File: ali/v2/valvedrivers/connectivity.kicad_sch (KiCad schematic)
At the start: 27 parts, among them J7 Conn_01x03, J8 Vertical Ethernet, U4 TJA1462ATK, U5 LAN8742AI, Y2 25 MHz

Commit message: Globally remove LCSC labels, update MPNs and IOCs, add +5V monitoring to DAQs, fix some footprints
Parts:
- C24: MPN GRM21A5C2J471FWA1 -> GRM1885C1H471JA01
- C26: MPN GRM21AR72A224KAC5 -> GRM188R71H224KAC4
- J8: LCSC C34677 -> (none)
- R17, R19: MPN RC0603FR-0710KL -> RC0603FR-0710KL
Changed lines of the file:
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@@
 			)
 		)
-		(property "MPN" " RC0603FR-0710KL"
+		(property "MPN" "RC0603FR-0710KL"
 			(at 53.34 85.09 90)
 			(hide yes)
@@
 			)
 		)
-		(property "LCSC" "C34677"
-			(at 187.96 121.92 0)
-			(hide yes)
-			(show_name no)
-			(do_not_autoplace no)
-			(effects
-				(font
-					(size 1.27 1.27)
-				)
-			)
-		)
 		(pin "1"
 		)
@@
 			)
 		)
-		(property "MPN" "GRM21AR72A224KAC5"
+		(property "MPN" "GRM188R71H224KAC4"
 			(at 157.48 132.08 0)
 			(hide yes)
@@
 			)
 		)
-		(property "MPN" "GRM21A5C2J471FWA1"
+		(property "MPN" "GRM1885C1H471JA01"
 			(at 100.33 50.8 0)
 			(hide yes)
@@
 			)
 		)
-		(property "MPN" " RC0603FR-0710KL"
+		(property "MPN" "RC0603FR-0710KL"
 			(at 99.06 102.87 0)
 			(hide yes)

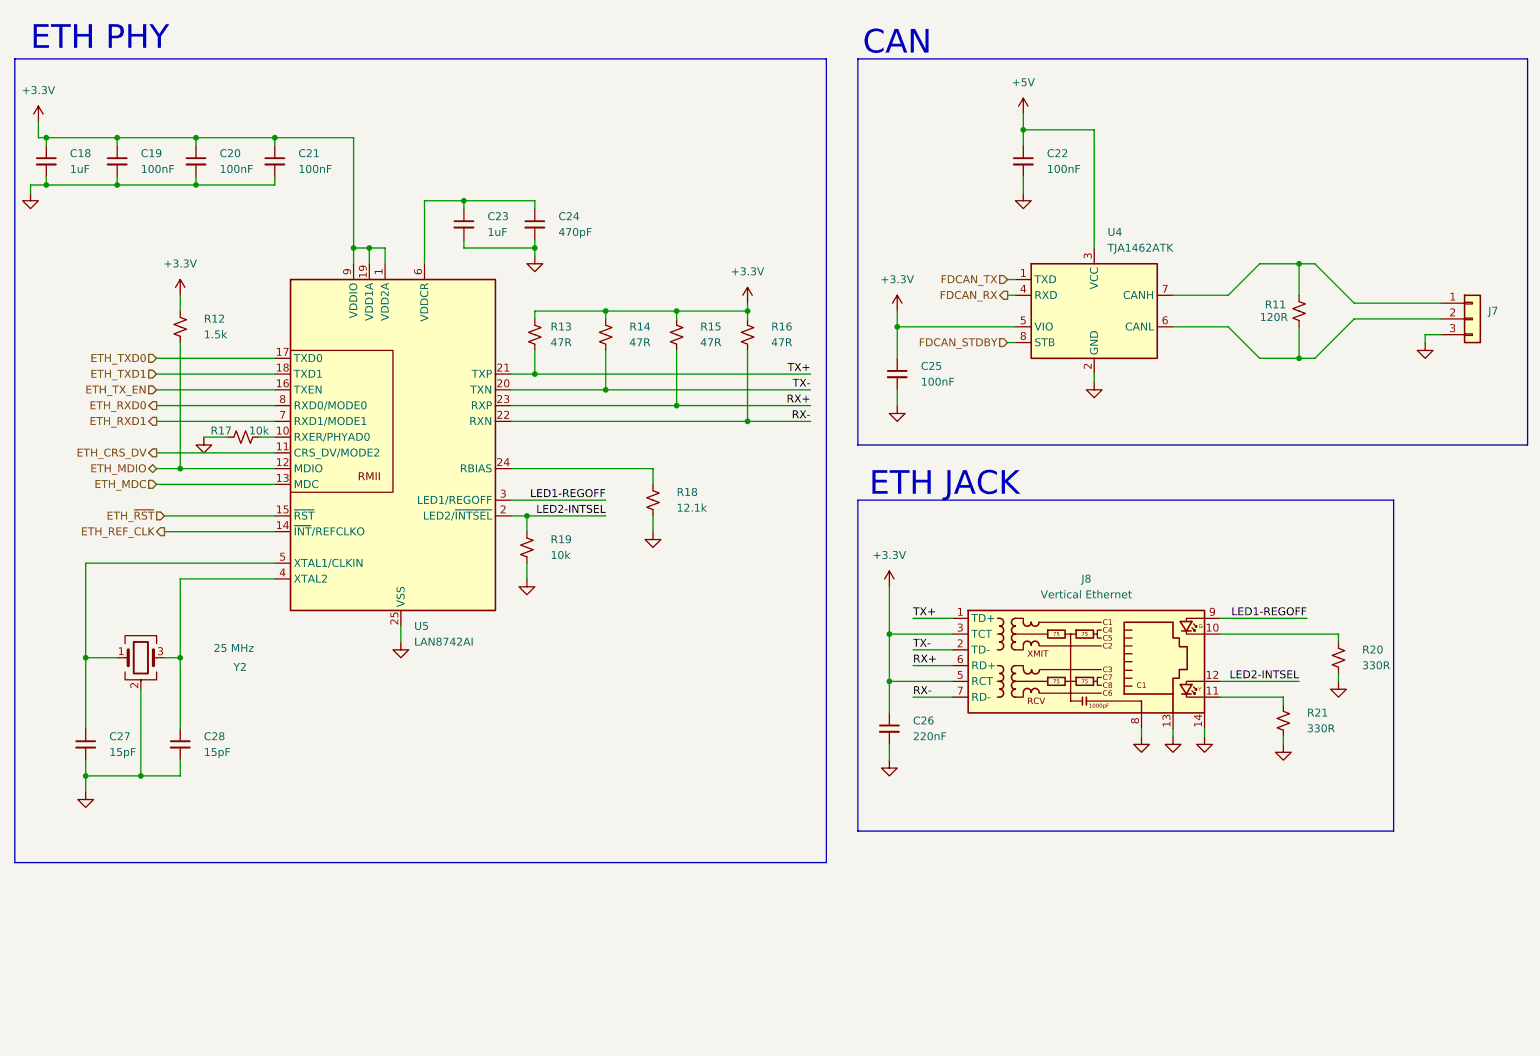
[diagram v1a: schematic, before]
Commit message: the great flatpak and kicad 10.0.6 migration
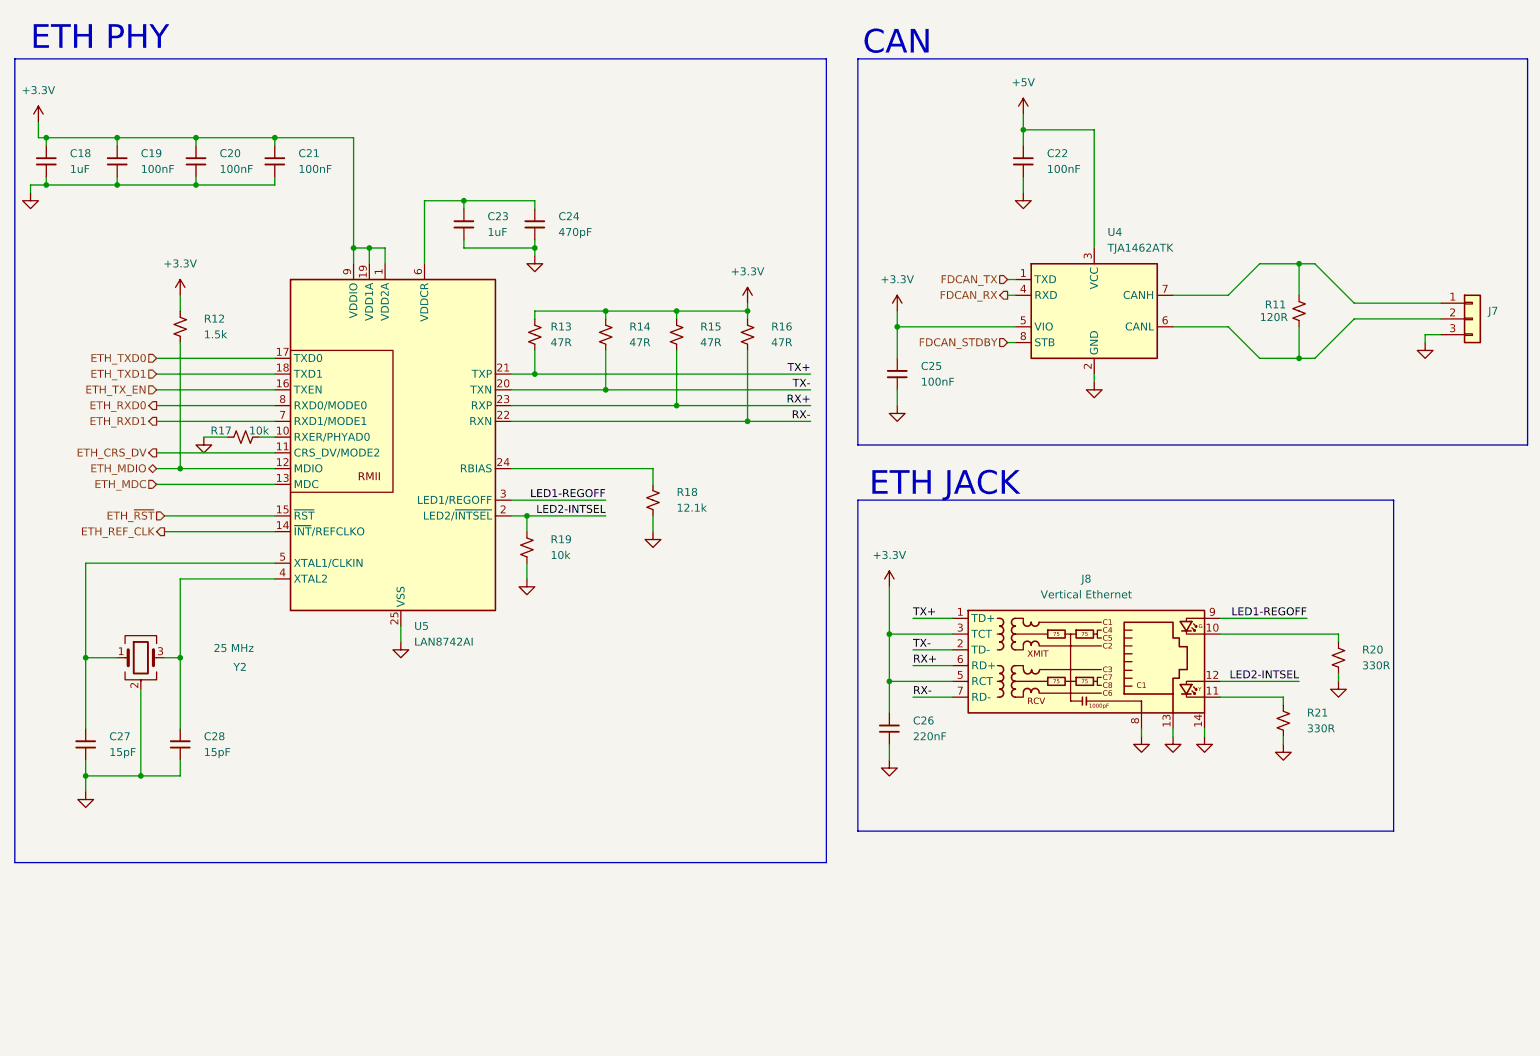
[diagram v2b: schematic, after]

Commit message: Add ignition port to valve driver board, set up CANBUS keepouts
Daniel please don't see this I am embarassed
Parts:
- renumbered J7 to J8, J8 to J9
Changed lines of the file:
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@@
 		(dnp no)
 		(fields_autoplaced yes)
-		(property "Reference" "#PWR045"
+		(property "Reference" "#PWR048"
 			(at 158.75 68.58 0)
 			(hide yes)
@@
 			(project "valvedrivers"
 				(path "/0eb5ae8a-84ea-4b7e-bec4-bb4e0217d666/c277875e-7a4a-49a6-a853-f4b1010be12e"
-					(reference "#PWR045")
+					(reference "#PWR048")
 					(unit 1)
 				)
@@
 		(dnp no)
 		(fields_autoplaced yes)
-		(property "Reference" "#PWR043"
+		(property "Reference" "#PWR046"
 			(at 43.18 66.04 0)
 			(hide yes)
@@
 			(project "valvedrivers"
 				(path "/0eb5ae8a-84ea-4b7e-bec4-bb4e0217d666/c277875e-7a4a-49a6-a853-f4b1010be12e"
-					(reference "#PWR043")
+					(reference "#PWR046")
 					(unit 1)
 				)
@@
 		(dnp no)
 		(fields_autoplaced yes)
-		(property "Reference" "#PWR060"
+		(property "Reference" "#PWR063"
 			(at 27.94 148.59 0)
 			(hide yes)
@@
 			(project "valvedrivers"
 				(path "/0eb5ae8a-84ea-4b7e-bec4-bb4e0217d666/c277875e-7a4a-49a6-a853-f4b1010be12e"
-					(reference "#PWR060")
+					(reference "#PWR063")
 					(unit 1)
 				)
@@
 		(dnp no)
 		(fields_autoplaced yes)
-		(property "Reference" "#PWR039"
+		(property "Reference" "#PWR042"
 			(at 20.32 38.1 0)
 			(hide yes)
@@
 			(project "valvedrivers"
 				(path "/0eb5ae8a-84ea-4b7e-bec4-bb4e0217d666/c277875e-7a4a-49a6-a853-f4b1010be12e"
-					(reference "#PWR039")
+					(reference "#PWR042")
 					(unit 1)
 				)
@@
 		(dnp no)
 		(fields_autoplaced yes)
-		(property "Reference" "#PWR056"
+		(property "Reference" "#PWR059"
 			(at 203.2 139.7 0)
 			(hide yes)
@@
 			(project "valvedrivers"
 				(path "/0eb5ae8a-84ea-4b7e-bec4-bb4e0217d666/c277875e-7a4a-49a6-a853-f4b1010be12e"
-					(reference "#PWR056")
+					(reference "#PWR059")
 					(unit 1)
 				)
@@
 		(dnp no)
 		(fields_autoplaced yes)
-		(property "Reference" "#PWR053"
+		(property "Reference" "#PWR056"
 			(at 78.74 124.46 0)
 			(hide yes)
@@
 			(project "valvedrivers"
 				(path "/0eb5ae8a-84ea-4b7e-bec4-bb4e0217d666/c277875e-7a4a-49a6-a853-f4b1010be12e"
-					(reference "#PWR053")
+					(reference "#PWR056")
 					(unit 1)
 				)
@@
 		(dnp no)
 		(fields_autoplaced yes)
-		(property "Reference" "#PWR048"
+		(property "Reference" "#PWR051"
 			(at 158.75 86.36 0)
 			(hide yes)
@@
 			(project "valvedrivers"
 				(path "/0eb5ae8a-84ea-4b7e-bec4-bb4e0217d666/c277875e-7a4a-49a6-a853-f4b1010be12e"
-					(reference "#PWR048")
+					(reference "#PWR051")
 					(unit 1)
 				)
@@
 		(dnp no)
 		(fields_autoplaced yes)
-		(property "Reference" "J7"
+		(property "Reference" "J8"
 			(at 254 64.7699 0)
 			(show_name no)
@@
 			(project "valvedrivers"
 				(path "/0eb5ae8a-84ea-4b7e-bec4-bb4e0217d666/c277875e-7a4a-49a6-a853-f4b1010be12e"
-					(reference "J7")
+					(reference "J8")
 					(unit 1)
 				)
@@
 		(dnp no)
 		(fields_autoplaced yes)
-		(property "Reference" "#PWR046"
+		(property "Reference" "#PWR049"
 			(at 243.84 76.2 0)
 			(hide yes)
@@
 			(project "valvedrivers"
 				(path "/0eb5ae8a-84ea-4b7e-bec4-bb4e0217d666/c277875e-7a4a-49a6-a853-f4b1010be12e"
-					(reference "#PWR046")
+					(reference "#PWR049")
 					(unit 1)
 				)
@@
 		(dnp no)
 		(fields_autoplaced yes)
-		(property "Reference" "J8"
+		(property "Reference" "J9"
 			(at 189.23 107.95 0)
 			(show_name no)
@@
 			(project "valvedrivers"
 				(path "/0eb5ae8a-84ea-4b7e-bec4-bb4e0217d666/c277875e-7a4a-49a6-a853-f4b1010be12e"
-					(reference "J8")
+					(reference "J9")
 					(unit 1)
 				)
@@
 		(dnp no)
 		(fields_autoplaced yes)
-		(property "Reference" "#PWR042"
+		(property "Reference" "#PWR045"
 			(at 100.33 62.23 0)
 			(hide yes)
@@
 			(project "valvedrivers"
 				(path "/0eb5ae8a-84ea-4b7e-bec4-bb4e0217d666/c277875e-7a4a-49a6-a853-f4b1010be12e"
-					(reference "#PWR042")
+					(reference "#PWR045")
 					(unit 1)
 				)
@@
 		(dnp no)
 		(fields_autoplaced yes)
-		(property "Reference" "#PWR047"
+		(property "Reference" "#PWR050"
 			(at 190.5 82.55 0)
 			(hide yes)
@@
 			(project "valvedrivers"
 				(path "/0eb5ae8a-84ea-4b7e-bec4-bb4e0217d666/c277875e-7a4a-49a6-a853-f4b1010be12e"
-					(reference "#PWR047")
+					(reference "#PWR050")
 					(unit 1)
 				)
@@
 		(dnp no)
 		(fields_autoplaced yes)
-		(property "Reference" "#PWR041"
+		(property "Reference" "#PWR044"
 			(at 179.07 52.07 0)
 			(hide yes)
@@
 			(project "valvedrivers"
 				(path "/0eb5ae8a-84ea-4b7e-bec4-bb4e0217d666/c277875e-7a4a-49a6-a853-f4b1010be12e"
-					(reference "#PWR041")
+					(reference "#PWR044")
 					(unit 1)
 				)
@@
 		(dnp no)
 		(fields_autoplaced yes)
-		(property "Reference" "#PWR059"
+		(property "Reference" "#PWR062"
 			(at 157.48 143.51 0)
 			(hide yes)
@@
 			(project "valvedrivers"
 				(path "/0eb5ae8a-84ea-4b7e-bec4-bb4e0217d666/c277875e-7a4a-49a6-a853-f4b1010be12e"
-					(reference "#PWR059")
+					(reference "#PWR062")
 					(unit 1)
 				)
@@
 		(dnp no)
 		(fields_autoplaced yes)
-		(property "Reference" "#PWR050"
+		(property "Reference" "#PWR053"
 			(at 119.38 106.68 0)
 			(hide yes)
@@
 			(project "valvedrivers"
 				(path "/0eb5ae8a-84ea-4b7e-bec4-bb4e0217d666/c277875e-7a4a-49a6-a853-f4b1010be12e"
-					(reference "#PWR050")
+					(reference "#PWR053")
 					(unit 1)
 				)
@@
 		(dnp no)
 		(fields_autoplaced yes)
-		(property "Reference" "#PWR057"
+		(property "Reference" "#PWR060"
 			(at 208.28 139.7 0)
 			(hide yes)
@@
 			(project "valvedrivers"
 				(path "/0eb5ae8a-84ea-4b7e-bec4-bb4e0217d666/c277875e-7a4a-49a6-a853-f4b1010be12e"
-					(reference "#PWR057")
+					(reference "#PWR060")
 					(unit 1)
 				)
@@
 		(dnp no)
 		(fields_autoplaced yes)
-		(property "Reference" "#PWR051"
+		(property "Reference" "#PWR054"
 			(at 99.06 114.3 0)
 			(hide yes)
@@
 			(project "valvedrivers"
 				(path "/0eb5ae8a-84ea-4b7e-bec4-bb4e0217d666/c277875e-7a4a-49a6-a853-f4b1010be12e"
-					(reference "#PWR051")
+					(reference "#PWR054")
 					(unit 1)
 				)
@@
 		(dnp no)
 		(fields_autoplaced yes)
-		(property "Reference" "#PWR038"
+		(property "Reference" "#PWR041"
 			(at 179.07 36.83 0)
 			(hide yes)
@@
 			(project "valvedrivers"
 				(path "/0eb5ae8a-84ea-4b7e-bec4-bb4e0217d666/c277875e-7a4a-49a6-a853-f4b1010be12e"
-					(reference "#PWR038")
+					(reference "#PWR041")
 					(unit 1)
 				)
@@
 		(dnp no)
 		(fields_autoplaced yes)
-		(property "Reference" "#PWR054"
+		(property "Reference" "#PWR057"
 			(at 229.87 130.81 0)
 			(hide yes)
@@
 			(project "valvedrivers"
 				(path "/0eb5ae8a-84ea-4b7e-bec4-bb4e0217d666/c277875e-7a4a-49a6-a853-f4b1010be12e"
-					(reference "#PWR054")
+					(reference "#PWR057")
 					(unit 1)
 				)
@@
 		(dnp no)
 		(fields_autoplaced yes)
-		(property "Reference" "#PWR049"
+		(property "Reference" "#PWR052"
 			(at 46.99 91.44 0)
 			(hide yes)
@@
 			(project "valvedrivers"
 				(path "/0eb5ae8a-84ea-4b7e-bec4-bb4e0217d666/c277875e-7a4a-49a6-a853-f4b1010be12e"
-					(reference "#PWR049")
+					(reference "#PWR052")
 					(unit 1)
 				)
@@
 		(dnp no)
 		(fields_autoplaced yes)
-		(property "Reference" "#PWR058"
+		(property "Reference" "#PWR061"
 			(at 220.98 140.97 0)
 			(hide yes)
@@
 			(project "valvedrivers"
 				(path "/0eb5ae8a-84ea-4b7e-bec4-bb4e0217d666/c277875e-7a4a-49a6-a853-f4b1010be12e"
-					(reference "#PWR058")
+					(reference "#PWR061")
 					(unit 1)
 				)
@@
 		(dnp no)
 		(fields_autoplaced yes)
-		(property "Reference" "#PWR055"
+		(property "Reference" "#PWR058"
 			(at 198.12 139.7 0)
 			(hide yes)
@@
 			(project "valvedrivers"
 				(path "/0eb5ae8a-84ea-4b7e-bec4-bb4e0217d666/c277875e-7a4a-49a6-a853-f4b1010be12e"
-					(reference "#PWR055")
+					(reference "#PWR058")
 					(unit 1)
 				)
@@
 		(dnp no)
 		(fields_autoplaced yes)
-		(property "Reference" "#PWR052"
+		(property "Reference" "#PWR055"
 			(at 157.48 113.03 0)
 			(hide yes)
@@
 			(project "valvedrivers"
 				(path "/0eb5ae8a-84ea-4b7e-bec4-bb4e0217d666/c277875e-7a4a-49a6-a853-f4b1010be12e"
-					(reference "#PWR052")
+					(reference "#PWR055")
 					(unit 1)
 				)
@@
 		(dnp no)
 		(fields_autoplaced yes)
-		(property "Reference" "#PWR040"
+		(property "Reference" "#PWR043"
 			(at 19.05 52.07 0)
 			(hide yes)
@@
 			(project "valvedrivers"
 				(path "/0eb5ae8a-84ea-4b7e-bec4-bb4e0217d666/c277875e-7a4a-49a6-a853-f4b1010be12e"
-					(reference "#PWR040")
+					(reference "#PWR043")
 					(unit 1)
 				)
@@
 		(dnp no)
 		(fields_autoplaced yes)
-		(property "Reference" "#PWR044"
+		(property "Reference" "#PWR047"
 			(at 134.62 67.31 0)
 			(hide yes)
@@
 			(project "valvedrivers"
 				(path "/0eb5ae8a-84ea-4b7e-bec4-bb4e0217d666/c277875e-7a4a-49a6-a853-f4b1010be12e"
-					(reference "#PWR044")
+					(reference "#PWR047")
 					(unit 1)
 				)

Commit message: Fix 50R/60R widths
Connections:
- net CAN+: now reaches J8.1 (Pin_1), R11.2, U4.7 (CANH)
- net CAN-: now reaches J8.2 (Pin_2), R11.1, U4.6 (CANL)
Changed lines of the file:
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@@
+		)
+	)
+	(label "CAN-"
+		(at 205.7332 67.31 0)
+		(effects
+			(font
+				(size 1.27 1.27)
+			)
+			(justify left bottom)
 		)
 	)
@@
 		)
 	)
+	(label "CAN+"
+		(at 205.74 62.23 0)
+		(effects
+			(font
+				(size 1.27 1.27)
+			)
+			(justify left bottom)
+		)
+	)

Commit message: Begin prep for second board review
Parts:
- removed C26: 220nF, APRL_Passive:C_0603, symbol Device:C_Small
- removed J9: Vertical Ethernet, APRL_Connector:RJ45_Hanrun_HY951180A_Vertical, symbol APRL_Connector:RJ45_Hanrun_HY951180A
- removed R18: 12.1k, APRL_Passive:R_0603, symbol Device:R_Small_US
- removed R20: 330R, APRL_Passive:R_0603, symbol Device:R_Small_US
- added C24: 220nF, APRL_Passive:C_0603, symbol Device:C_Small
- added J8: Vertical Ethernet, APRL_Connector:RJ45_Hanrun_HY951180A_Vertical, symbol APRL_Connector:RJ45_Hanrun_HY951180A
- added R19: 12.1k, APRL_Passive:R_0603, symbol Device:R_Small_US
- added R22: 330R, APRL_Passive:R_0603, symbol Device:R_Small_US
- renumbered C23 to C22, C24 to C23, C27 to C25, C28 to C26, C22 to C27, C25 to C28, J8 to J9, R12 to R13, R13 to R14, R14 to R15, R15 to R16, R16 to R17, R17 to R18, R19 to R20, R11 to R23, U4 to U6
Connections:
- net +3.3V: now also C24.1, J8.3 (TCT), J8.5 (RCT)
- net GND: now also C24.2, J8.13, J8.14, J8.8, R19.2, R22.2
- net at R21.1: now also J8.10
- net at U5.24 (RBIAS): now also R19.1
- net CAN+: no longer names the net of J9.1 (Pin_1), R23.2, U6.7 (CANH)
- net CAN-: no longer names the net of J9.2 (Pin_2), R23.1, U6.6 (CANL)
- net LED1-REGOFF: no longer names the net of U5.3 (LED1/REGOFF)
- net LED1-REGOFF: now also J8.9
- net LED2-INTSEL: no longer names the net of R20.1, U5.2 (LED2/~{INTSEL})
- net LED2-INTSEL: now also J8.12
- net RX+: no longer names the net of R16.2, U5.23 (RXP)
- net RX+: now also J8.6 (RD+)
- net RX-: no longer names the net of R17.2, U5.22 (RXN)
- net RX-: now also J8.7 (RD-)
- net TX+: no longer names the net of R14.2, U5.21 (TXP)
- net TX+: now also J8.1 (TD+)
- net TX-: no longer names the net of R15.2, U5.20 (TXN)
- net TX-: now also J8.2 (TD-)
- new net: J8.11, R22.1
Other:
- note added: "ETH"
- note removed: "ETH JACK"
- note removed: "ETH PHY"
- moved on the sheet: C27, C28, J9, R15, R16, R17, R20, R23, U6
